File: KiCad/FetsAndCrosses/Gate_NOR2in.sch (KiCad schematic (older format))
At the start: 4 parts, among them Q38 2N7002, Q39 BSS84, Q40 BSS84, Q41 2N7002

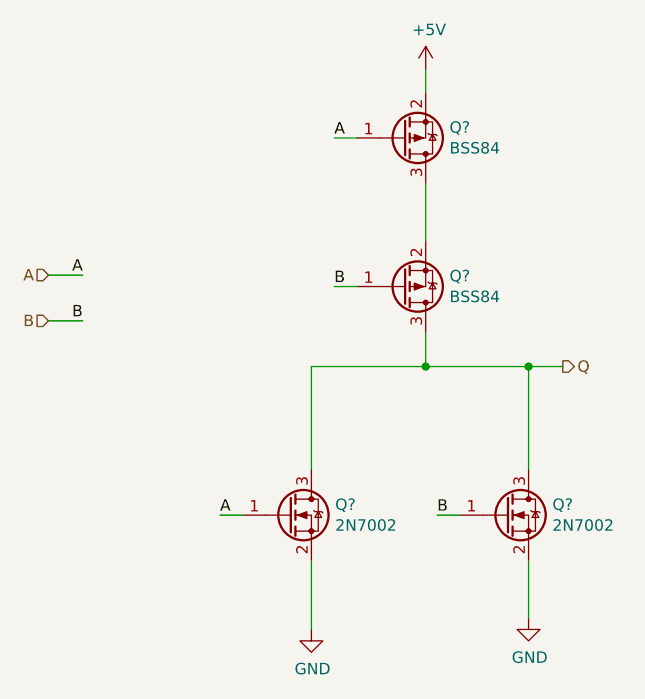
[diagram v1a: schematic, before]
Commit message: Schematic Done, Footprints assigned, ERC OK.
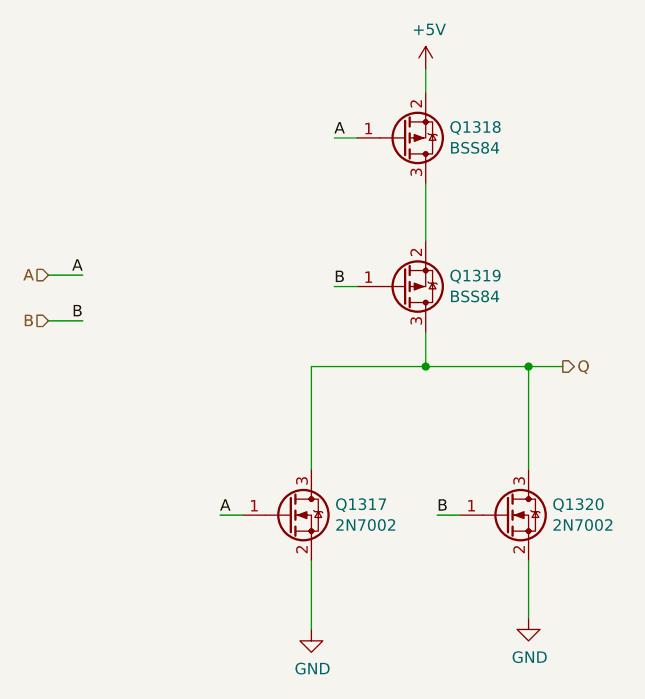
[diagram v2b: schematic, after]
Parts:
- Q493: renamed from Q38; footprint (none) -> LogicQ:SOT-23-N
- Q494: renamed from Q39; footprint (none) -> LogicQ:SOT-23-P
- Q495: renamed from Q40; footprint (none) -> LogicQ:SOT-23-P
- Q496: renamed from Q41; footprint (none) -> LogicQ:SOT-23-N

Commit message: Schematic fixes.
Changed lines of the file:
@@
 $Descr A4 11693 8268
 encoding utf-8
-Sheet 62 389
+Sheet 244 389
 Title ""
-Date ""
-Rev ""
-Comp ""
-Comment1 ""
+Date "2020-07-05"
+Rev "v0.0"
+Comp "Philipp Schilk"
+Comment1 "c"
 Comment2 ""
 Comment3 ""
@@
 AR Path="/5FB775FE/5F1827D4/5F172B07/5E56263B/5E557A8F" Ref="Q1319"  Part="1"
 AR Path="/5E553405/5F22E6FE/5E56263B/5E557A8F" Ref="Q659"  Part="1"
-F 0 "Q1319" H 5304 2454 50  0000 L CNN
+F 0 "Q875" H 5304 2454 50  0000 L CNN
 F 1 "BSS84" H 5304 2545 50  0000 L CNN
 F 2 "LogicQ:SOT-23-P" H 5300 2600 50  0001 C CNN
@@
 AR Path="/5FB775FE/5F1827D4/5F172B07/5E56263B/5E557A95" Ref="Q1317"  Part="1"
 AR Path="/5E553405/5F22E6FE/5E56263B/5E557A95" Ref="Q657"  Part="1"
-F 0 "Q1317" H 4804 3546 50  0000 L CNN
+F 0 "Q873" H 4804 3546 50  0000 L CNN
 F 1 "2N7002" H 4804 3455 50  0000 L CNN
 F 2 "LogicQ:SOT-23-N" H 4800 3600 50  0001 C CNN
@@
 AR Path="/5FB775FE/5F1827D4/5F172B07/5E56263B/5E557A9B" Ref="Q1318"  Part="1"
 AR Path="/5E553405/5F22E6FE/5E56263B/5E557A9B" Ref="Q658"  Part="1"
-F 0 "Q1318" H 5304 1804 50  0000 L CNN
+F 0 "Q874" H 5304 1804 50  0000 L CNN
 F 1 "BSS84" H 5304 1895 50  0000 L CNN
 F 2 "LogicQ:SOT-23-P" H 5300 1950 50  0001 C CNN
@@
 AR Path="/5FB775FE/5F1827D4/5F172B07/5E56263B/5E557AA1" Ref="Q1320"  Part="1"
 AR Path="/5E553405/5F22E6FE/5E56263B/5E557AA1" Ref="Q660"  Part="1"
-F 0 "Q1320" H 5754 3546 50  0000 L CNN
+F 0 "Q876" H 5754 3546 50  0000 L CNN
 F 1 "2N7002" H 5754 3455 50  0000 L CNN
 F 2 "LogicQ:SOT-23-N" H 5750 3600 50  0001 C CNN

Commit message: First Draft Schematic Updates
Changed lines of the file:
@@
 $Descr A4 11693 8268
 encoding utf-8
-Sheet 244 389
+Sheet 244 360
 Title ""
 Date "2020-07-05"
@@
 AR Path="/5FB775FE/5F1827D4/5F172B07/5E56263B/5E557A8F" Ref="Q1319"  Part="1"
 AR Path="/5E553405/5F22E6FE/5E56263B/5E557A8F" Ref="Q659"  Part="1"
-F 0 "Q875" H 5304 2454 50  0000 L CNN
+F 0 "Q887" H 5304 2454 50  0000 L CNN
 F 1 "BSS84" H 5304 2545 50  0000 L CNN
 F 2 "LogicQ:SOT-23-P" H 5300 2600 50  0001 C CNN
@@
 AR Path="/5FB775FE/5F1827D4/5F172B07/5E56263B/5E557A95" Ref="Q1317"  Part="1"
 AR Path="/5E553405/5F22E6FE/5E56263B/5E557A95" Ref="Q657"  Part="1"
-F 0 "Q873" H 4804 3546 50  0000 L CNN
+F 0 "Q885" H 4804 3546 50  0000 L CNN
 F 1 "2N7002" H 4804 3455 50  0000 L CNN
 F 2 "LogicQ:SOT-23-N" H 4800 3600 50  0001 C CNN
@@
 AR Path="/5FB775FE/5F1827D4/5F172B07/5E56263B/5E557A9B" Ref="Q1318"  Part="1"
 AR Path="/5E553405/5F22E6FE/5E56263B/5E557A9B" Ref="Q658"  Part="1"
-F 0 "Q874" H 5304 1804 50  0000 L CNN
+F 0 "Q886" H 5304 1804 50  0000 L CNN
 F 1 "BSS84" H 5304 1895 50  0000 L CNN
 F 2 "LogicQ:SOT-23-P" H 5300 1950 50  0001 C CNN
@@
 AR Path="/5FB775FE/5F1827D4/5F172B07/5E56263B/5E557AAE" Ref="#PWR0930"  Part="1"
 AR Path="/5E553405/5F22E6FE/5E56263B/5E557AAE" Ref="#PWR0494"  Part="1"
-F 0 "#PWR0930" H 5650 3700 50  0001 C CNN
+F 0 "#PWR0653" H 5650 3700 50  0001 C CNN
 F 1 "GND" H 5655 3777 50  0000 C CNN
 F 2 "" H 5650 3950 50  0001 C CNN
@@
 AR Path="/5FB775FE/5F1827D4/5F172B07/5E56263B/5E557ABB" Ref="#PWR0931"  Part="1"
 AR Path="/5E553405/5F22E6FE/5E56263B/5E557ABB" Ref="#PWR0495"  Part="1"
-F 0 "#PWR0931" H 5200 1400 50  0001 C CNN
+F 0 "#PWR0654" H 5200 1400 50  0001 C CNN
 F 1 "+5V" H 5215 1723 50  0000 C CNN
 F 2 "" H 5200 1550 50  0001 C CNN
@@
 AR Path="/5FB775FE/5F1827D4/5F172B07/5E56263B/5E557AA1" Ref="Q1320"  Part="1"
 AR Path="/5E553405/5F22E6FE/5E56263B/5E557AA1" Ref="Q660"  Part="1"
-F 0 "Q876" H 5754 3546 50  0000 L CNN
+F 0 "Q888" H 5754 3546 50  0000 L CNN
 F 1 "2N7002" H 5754 3455 50  0000 L CNN
 F 2 "LogicQ:SOT-23-N" H 5750 3600 50  0001 C CNN
@@
 AR Path="/5FB775FE/5F1827D4/5F172B07/5E56263B/5E559196" Ref="#PWR0932"  Part="1"
 AR Path="/5E553405/5F22E6FE/5E56263B/5E559196" Ref="#PWR0496"  Part="1"
-F 0 "#PWR0932" H 4700 3750 50  0001 C CNN
+F 0 "#PWR0655" H 4700 3750 50  0001 C CNN
 F 1 "GND" H 4705 3827 50  0000 C CNN
 F 2 "" H 4700 4000 50  0001 C CNN
